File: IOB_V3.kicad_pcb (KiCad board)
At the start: 4 copper layers, 140 x 80 mm, 262 parts, among them J1 Conn_01x02, J10 Conn_01x04, J11 Conn_01x04, J12 Conn_01x04, J13 Conn_01x04, J14 Conn_01x04, J15 Conn_01x08, J16 Conn_02x04_Odd_Even, J17 Conn_01x04_MountingPin, J18 Conn_01x08, J19 Conn_01x04_MountingPin, J2 Conn_01x03, J3 Conn_01x04, J4 Conn_01x04, J5 Conn_01x04, J6 Conn_01x04, J7 Conn_01x04, J8 Conn_01x04, J9 Conn_01x04, Q1 BSZ0902NSATMA1, Q10 BSZ0902NSATMA1, Q11 BSZ0902NSATMA1, Q12 BSZ0902NSATMA1, Q13 SI2300, Q2 BSZ0902NSATMA1, Q3 BSZ0902NSATMA1, Q4 BSZ0902NSATMA1, Q5 BSZ0902NSATMA1, Q6 BSZ0902NSATMA1, Q7 BSZ0902NSATMA1, Q8 BSZ0902NSATMA1, Q9 BSZ0902NSATMA1, SW1 SW_Push_Dual, SW2 SW_Push_Dual, SW3 SW_DIP_x08, U1 REF3033, U10 INA180, U11 INA180, U12 INA180, U13 INA180, U14 TS30041, U15 MCP1700-3302E_SOT23, U16 CD74HC4067M, U17 MCP2562FD, U18 W25Q256JV, U19 STM32G474MET3, U2 INA180, U20 CD74HC4067M, U3 INA180, U4 INA180, U5 INA180, U6 INA180, U7 INA180, U8 INA180, U9 INA180, X1 TXC-7C

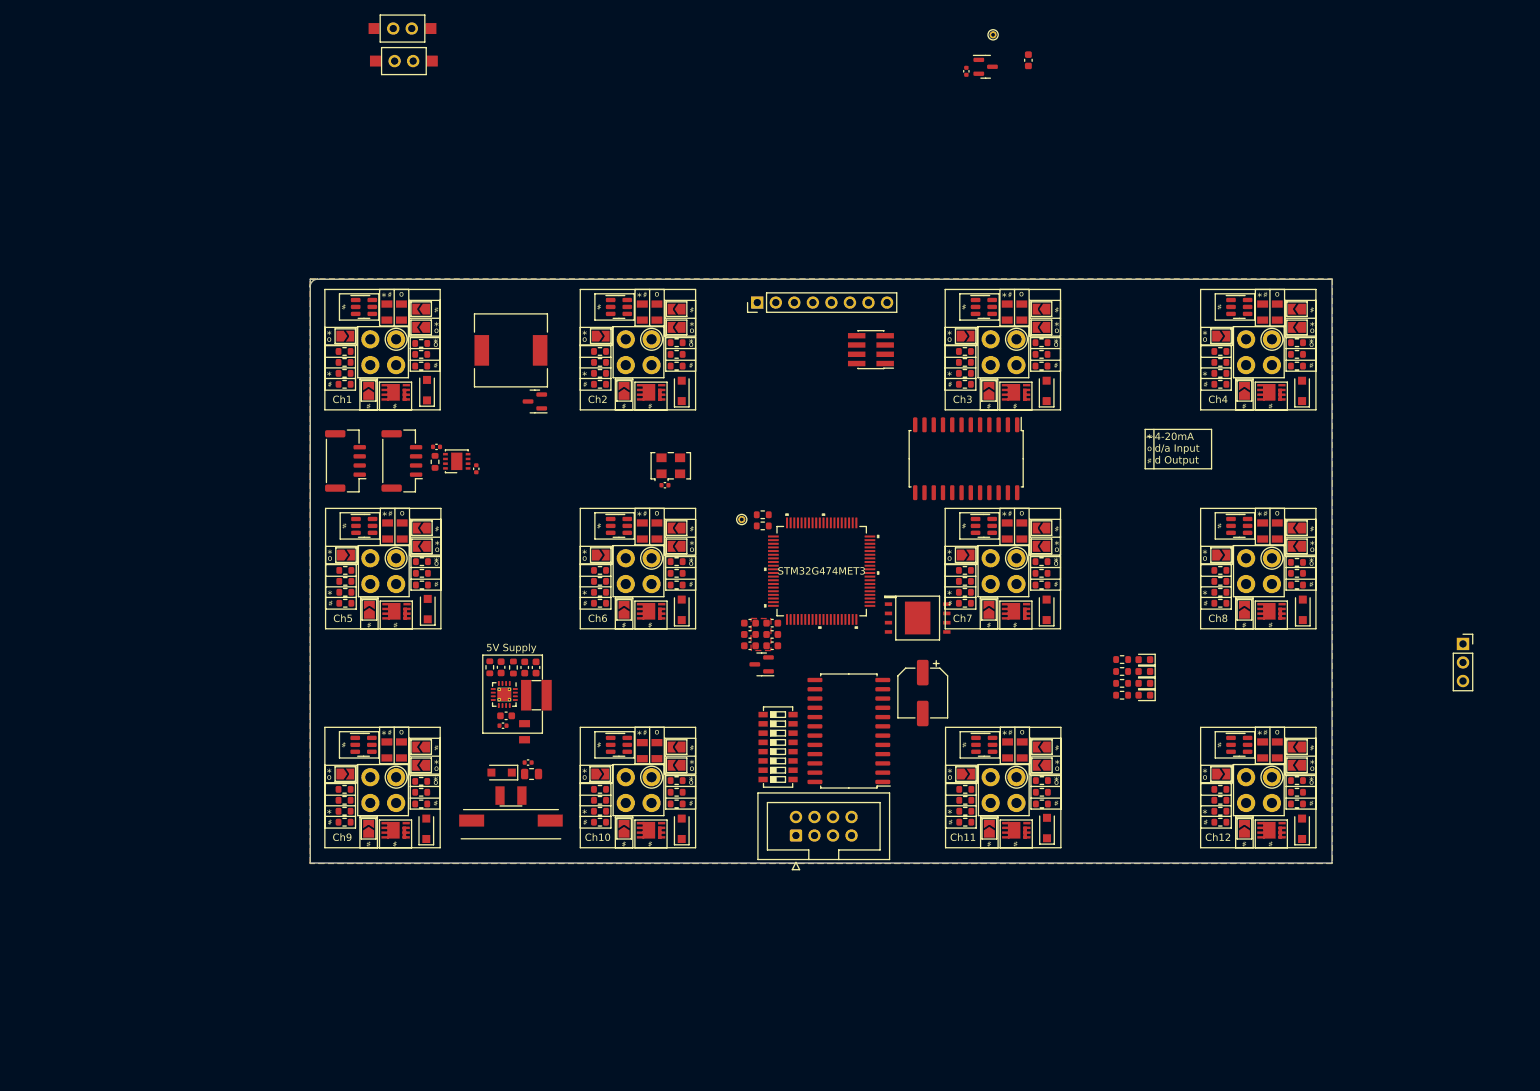
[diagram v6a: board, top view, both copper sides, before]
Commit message: Connectors change and part side flip
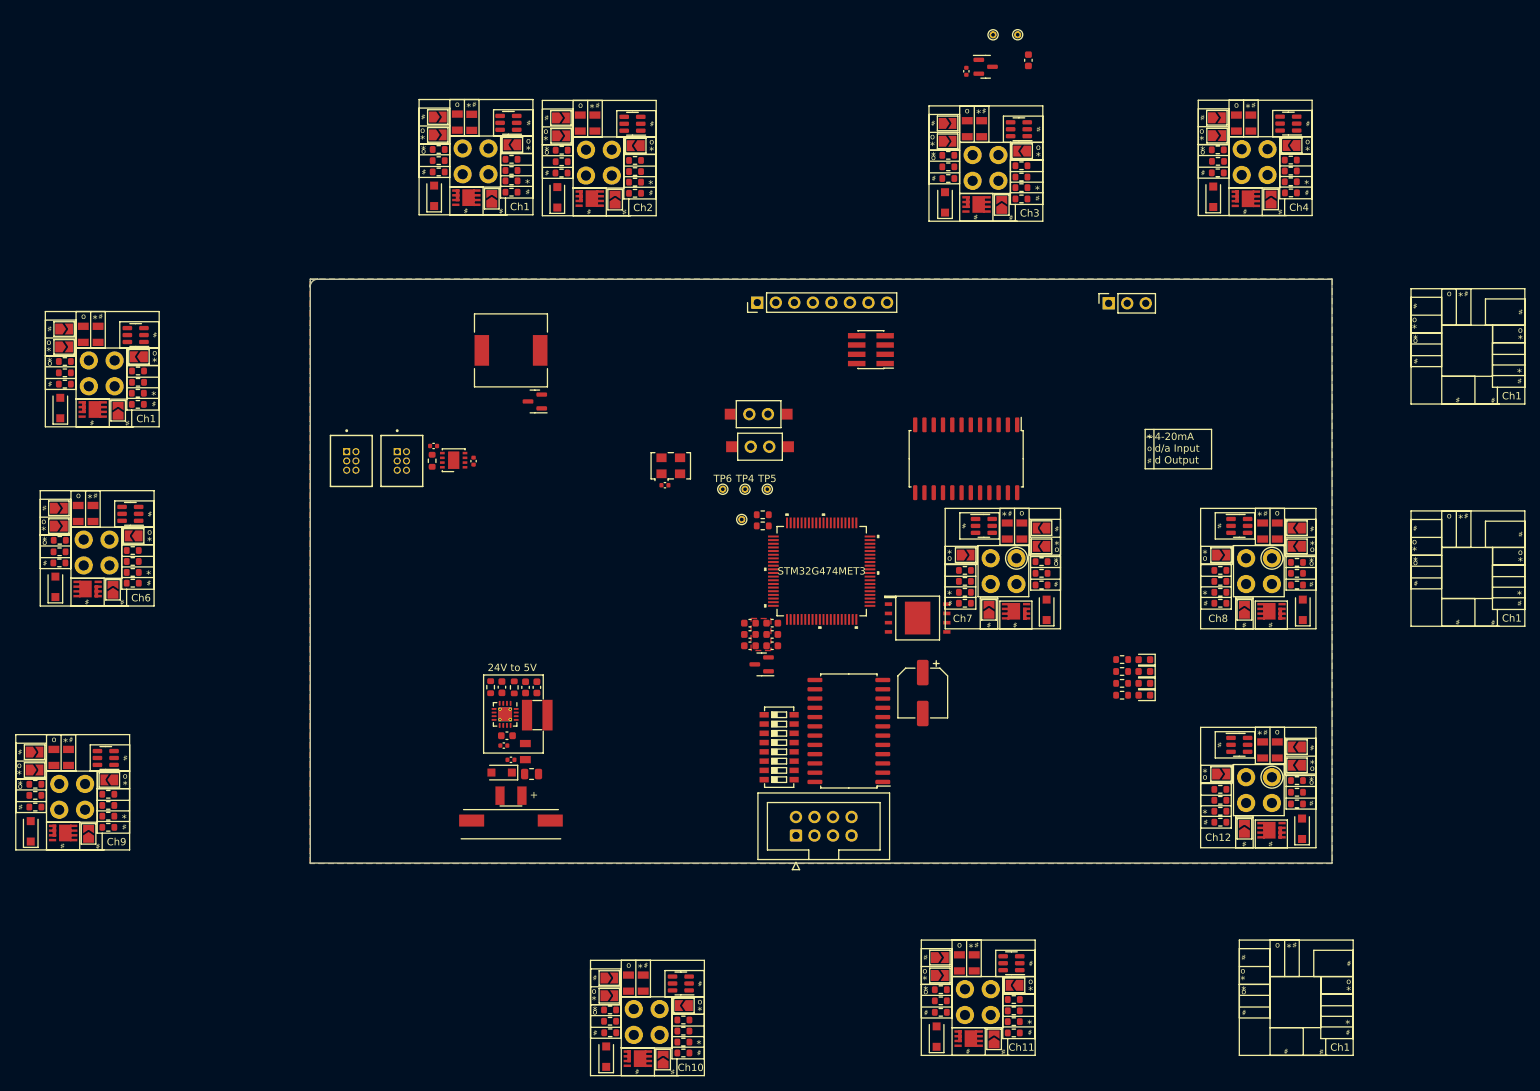
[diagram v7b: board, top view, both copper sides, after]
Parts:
- added TP3: TestPoint, TestPoint:TestPoint_THTPad_D1.0mm_Drill0.5mm, F.Cu at (176.9, 21.5)
- added TP4: TestPoint, TestPoint:TestPoint_THTPad_D1.0mm_Drill0.5mm, F.Cu at (139.6, 83.8)
- added TP5: TestPoint, TestPoint:TestPoint_THTPad_D1.0mm_Drill0.5mm, F.Cu at (142.6, 83.8)
- added TP6: TestPoint, TestPoint:TestPoint_THTPad_D1.0mm_Drill0.5mm, F.Cu at (136.5, 83.8)
- J11, J12, J13, J3, J4, J5, J6, J7, J8: moved to B.Cu
- J17, J19: value Conn_01x04_MountingPin -> TFC-103-01-F-D; footprint Connector_JST:JST_GH_BM04B-GHS-TBT_1x04-1MP_P1.25mm_Vertical -> TXV_Library_Footprints:SAMTEC_TFC-103-01-F-D
- moved D7 85.9 mm to (45.1, 97.2)
- moved JP35 84.7 mm to (45.5, 88.8), turned to 0 degrees
- moved JP36 84.7 mm to (45.5, 86.4), turned to 0 degrees
- moved R42 84.6 mm to (45.6, 93.9), turned to 180 degrees
- moved R39 84.6 mm to (45.6, 92.3), turned to 0 degrees
- moved R41 84.6 mm to (45.7, 90.8), turned to 0 degrees
- moved F11 79.3 mm to (48.2, 87.1)
- moved Q6 77.3 mm to (49.6, 97.5)
- moved F12 75.3 mm to (50.2, 87.1)
- moved J8 74.3 mm to (50.7, 92.5), turned to 180 degrees
- moved SW1 71.9 mm to (141.6, 78.0)
- moved SW2 71.9 mm to (141.4, 73.5)
- moved JP32 70.1 mm to (53.0, 97.5)
- moved J2 67.3 mm to (189.4, 58.3), turned to 90 degrees
- moved U7 67.0 mm to (55.4, 87.2), turned to 180 degrees
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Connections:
- net /MCU/GND1 renamed Net-(SW3-Pad9)
- net /MCU/GND2 renamed Net-(SW3-Pad10)
- net /MCU/GND3 renamed Net-(SW3-Pad11)
- net /MCU/GND4 renamed Net-(SW3-Pad12)
- net /MCU/GND5 renamed Net-(SW3-Pad13)
- net /MCU/GND6 renamed Net-(SW3-Pad14)
- net /MCU/GND7 renamed Net-(SW3-Pad15)
- net /MCU/GND8 renamed Net-(SW3-Pad16)
- U19 pad 2: unconnected-(U19-Pad2) -> Net-(TP6-Pad1)
- U19 pad 74: unconnected-(U19-Pad74) -> Net-(TP4-Pad1)
- U19 pad 8: unconnected-(U19-Pad8) -> Net-(TP5-Pad1)
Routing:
- added copper zone on In2.Cu, net +24V
- added copper zone on In1.Cu, net +3V3
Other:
- board text added: "+"
- board text added: "24V to 5V"
- board text removed: "5V Supply"
- board text removed: "Ch5"
